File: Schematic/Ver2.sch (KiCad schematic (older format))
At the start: 20 parts, among them IC1 ATMEGA328P-A, P1 PROG, P2 Power, P3 OLED, P4 DBG, SW1 SW_Push, U1 L78L05ABUTR

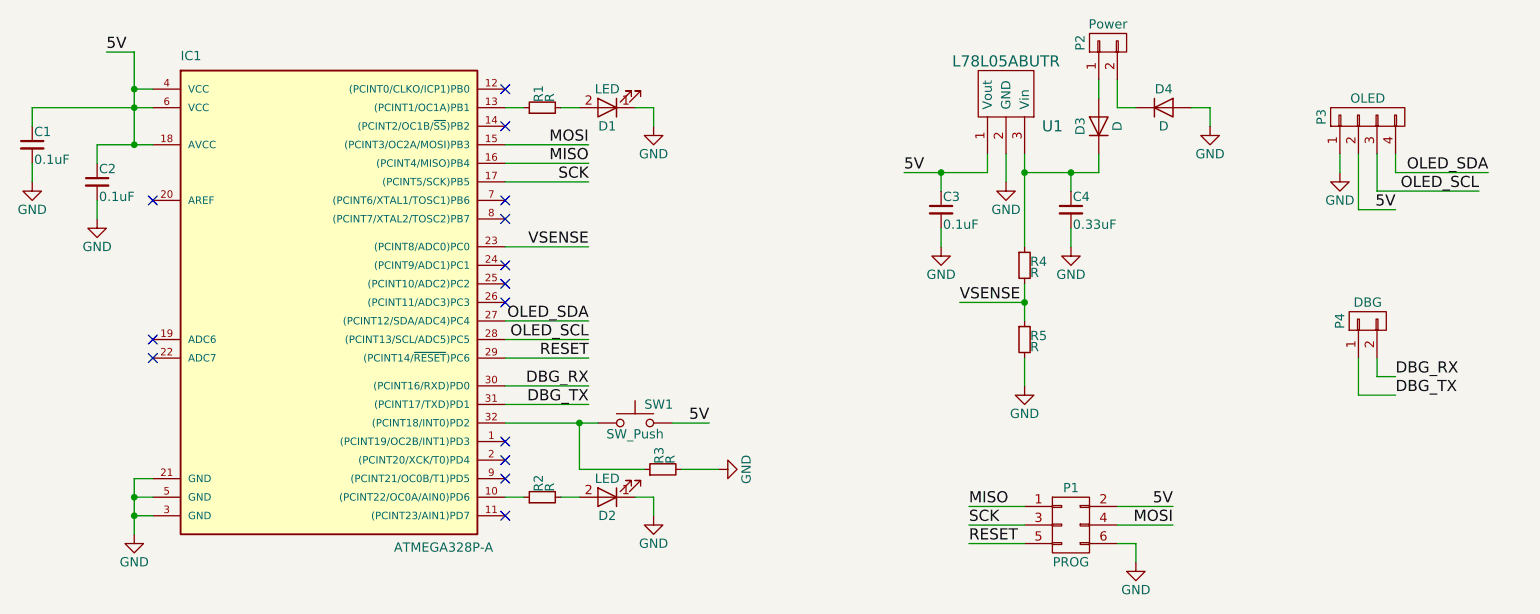
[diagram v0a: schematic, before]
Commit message: Added the tracks and completed the design
ordered the cars form OSH park
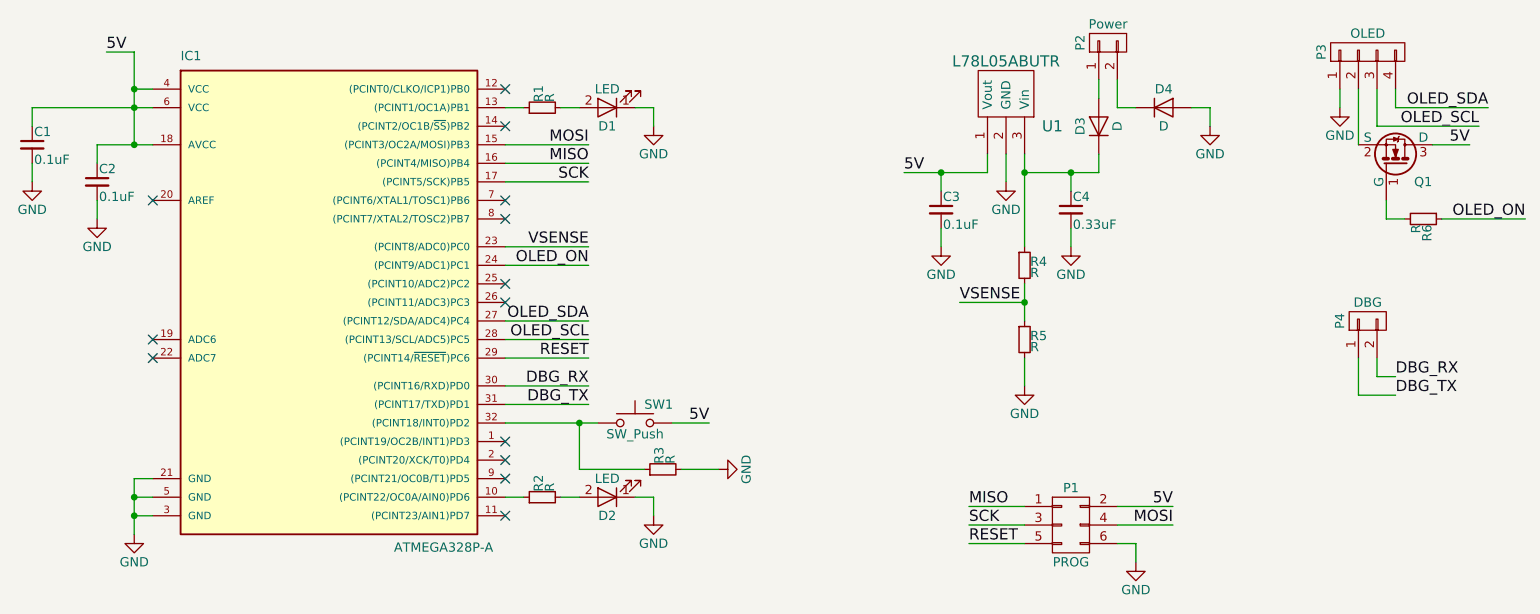
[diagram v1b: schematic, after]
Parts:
- added Q1: 2N7002, TO_SOT_Packages_SMD:SOT-23, symbol 2N7002
- added R6: R, Resistors_SMD:R_0805_HandSoldering, symbol R_Small
- P2: footprint Pin_Headers:Pin_Header_Straight_1x02_Pitch2.54mm -> Solderpads:2xSolderpads
- P3: footprint Pin_Headers:Pin_Header_Straight_2x02_Pitch2.54mm -> Solderpads:4xSolderpads
- P4: footprint Pin_Headers:Pin_Header_Straight_2x01_Pitch2.54mm -> Solderpads:2xSolderpads
- SW1: footprint Pin_Headers:Pin_Header_Straight_1x02_Pitch1.27mm -> Solderpads:2xSolderpads
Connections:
- net 5V: now also Q1.3 (D); no longer P3.2 (P2)
- net OLED_ON: now reaches IC1.24 ((PCINT9/ADC1)PC1)
- net OLED_ON: now also R6.1
- new net: P3.2 (P2), Q1.2 (S)
- new net: Q1.1 (G), R6.2
- no-connect marks 14 -> 13
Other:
- moved on the sheet: P3
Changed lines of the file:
@@
 LIBS:l78l05abutr
 LIBS:switches
+LIBS:Ver2-cache
 EELAYER 25 0
 EELAYER END
@@
 F 0 "P2" H 7750 2050 50  0000 C CNN
 F 1 "Power" V 7850 1900 50  0000 C CNN
-F 2 "Pin_Headers:Pin_Header_Straight_1x02_Pitch2.54mm" H 7750 1900 50  0001 C CNN
+F 2 "Solderpads:2xSolderpads" H 7750 1900 50  0001 C CNN
 F 3 "" H 7750 1900 50  0000 C CNN
 	1    7750 1900
@@
 L CONN_01X04 P3
 U 1 1 589E55C2
-P 9150 2300
-F 0 "P3" H 9150 2550 50  0000 C CNN
-F 1 "OLED" V 9250 2300 50  0000 C CNN
-F 2 "Pin_Headers:Pin_Header_Straight_2x02_Pitch2.54mm" H 9150 2300 50  0001 C CNN
-F 3 "" H 9150 2300 50  0000 C CNN
-	1    9150 2300
+P 9150 1950
+F 0 "P3" H 9150 2200 50  0000 C CNN
+F 1 "OLED" V 9250 1950 50  0000 C CNN
+F 2 "Solderpads:4xSolderpads" H 9150 1950 50  0001 C CNN
+F 3 "" H 9150 1950 50  0000 C CNN
+	1    9150 1950
 	0    -1   -1   0
 $EndComp
@@
 Text Label 4950 3500 2    60   ~ 0
 OLED_SCL
-Text Label 9800 2600 2    60   ~ 0
+Text Label 9800 2250 2    60   ~ 0
 OLED_SDA
-Text Label 9750 2700 2    60   ~ 0
+Text Label 9750 2350 2    60   ~ 0
 OLED_SCL
-Text Label 9300 2800 2    60   ~ 0
+Text Label 9700 2450 2    60   ~ 0
 5V
 $Comp
 L GND #PWR08
 U 1 1 589E5AFB
-P 9000 2600
-F 0 "#PWR08" H 9000 2350 50  0001 C CNN
-F 1 "GND" H 9000 2450 50  0000 C CNN
-F 2 "" H 9000 2600 50  0000 C CNN
-F 3 "" H 9000 2600 50  0000 C CNN
-	1    9000 2600
+P 9000 2250
+F 0 "#PWR08" H 9000 2000 50  0001 C CNN
+F 1 "GND" H 9000 2100 50  0000 C CNN
+F 2 "" H 9000 2250 50  0000 C CNN
+F 3 "" H 9000 2250 50  0000 C CNN
+	1    9000 2250
 	1    0    0    -1
 $EndComp
@@
 F 0 "SW1" H 5250 4050 50  0000 L CNN
 F 1 "SW_Push" H 5200 3890 50  0000 C CNN
-F 2 "Pin_Headers:Pin_Header_Straight_1x02_Pitch1.27mm" H 5200 4150 50  0001 C CNN
+F 2 "Solderpads:2xSolderpads" H 5200 4150 50  0001 C CNN
 F 3 "" H 5200 4150 50  0000 C CNN
 	1    5200 3950
@@
 F 0 "P4" H 9150 3550 50  0000 C CNN
 F 1 "DBG" V 9250 3400 50  0000 C CNN
-F 2 "Pin_Headers:Pin_Header_Straight_2x01_Pitch2.54mm" H 9150 3400 50  0001 C CNN
+F 2 "Solderpads:2xSolderpads" H 9150 3400 50  0001 C CNN
 F 3 "" H 9150 3400 50  0000 C CNN
 	1    9150 3400
@@
 	4950 3500 4500 3500
 Wire Wire Line
-	9300 2500 9300 2600
-Wire Wire Line
-	9300 2600 9800 2600
-Wire Wire Line
-	9200 2500 9200 2700
-Wire Wire Line
-	9200 2700 9750 2700
-Wire Wire Line
-	9100 2500 9100 2800
-Wire Wire Line
-	9100 2800 9300 2800
-Wire Wire Line
-	9000 2500 9000 2600
+	9300 2150 9300 2250
+Wire Wire Line
+	9300 2250 9800 2250
+Wire Wire Line
+	9200 2150 9200 2350
+Wire Wire Line
+	9200 2350 9750 2350
+Wire Wire Line
+	9100 2150 9100 2450
+Wire Wire Line
+	9000 2150 9000 2250
 Wire Wire Line
 	7700 2100 7700 2200
@@
 NoConn ~ 4500 2750
 NoConn ~ 4500 2850
-NoConn ~ 4500 3100
 NoConn ~ 4500 3200
 NoConn ~ 4500 3300
@@
 NoConn ~ 4500 4250
 NoConn ~ 4500 4450
+$Comp
+L 2N7002 Q1
+U 1 1 58A0CB9B
+P 9300 2550
+F 0 "Q1" V 9200 2650 50  0000 L CNN
+F 1 "2N7002" H 9500 2550 50  0001 L CNN
+F 2 "TO_SOT_Packages_SMD:SOT-23" H 9500 2475 50  0001 L CIN
+F 3 "" H 9300 2550 50  0000 L CNN
+F 4 "NTR5103N" V 9300 2550 60  0001 C CNN "Part number"
+	1    9300 2550
+	0    1    -1   0
+$EndComp
+Wire Wire Line
+	9700 2450 9500 2450
+Wire Wire Line
+	9250 2750 9250 2850
+Text Label 10000 2850 2    60   ~ 0
+OLED_ON
+$Comp
+L R_Small R6
+U 1 1 58A0E51B
+P 9450 2850
+F 0 "R6" H 9480 2870 50  0000 L CNN
+F 1 "R" H 9480 2810 50  0000 L CNN
+F 2 "Resistors_SMD:R_0805_HandSoldering" H 9450 2850 50  0001 C CNN
+F 3 "" H 9450 2850 50  0000 C CNN
+	1    9450 2850
+	0    1    1    0
+$EndComp
+Wire Wire Line
+	10000 2850 9550 2850
+Wire Wire Line
+	9250 2850 9350 2850
+Text Label 4950 3100 2    60   ~ 0
+OLED_ON
+Wire Wire Line
+	4950 3100 4500 3100
 $EndSCHEMATC

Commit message: Changed Partnumber on a resistor
Had to change to another component when ordering because component was
out of stock.
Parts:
- C1, C2, C3: Part number (none) -> 885012207072
- C4: Part number (none) -> 885012207048
- D1: Part number (none) -> APT3216EC
- D2: Part number (none) -> CMD15-21VGC/TR8
- Q1: Part number NTR5103N -> NTR5103NT1G
- R1, R2: value R -> 220; Part number (none) -> CRCW0805220RFKEA
- R3, R4: value R -> 10k; Part number (none) -> CRCW080510K0FKEA
- R5: value R -> 15k; Part number (none) -> CRCW080515K0JNEA
- R6: value R -> 1k; Part number (none) -> CRCW08051K00FKEA
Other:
- moved on the sheet: C3, C4, D3, D4, P1, P2, P3, P4, Q1, R4, R5, R6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
